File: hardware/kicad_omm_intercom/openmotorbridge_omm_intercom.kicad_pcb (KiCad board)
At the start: 2 copper layers, 60 x 30 mm, 19 parts, among them J1 TYPE-C-31-M-12_IP67, SW1 Power_MFB, SW2 Mesh_Group, SW3 Vol_Plus, SW4 Vol_Minus, U1 ESP32-C6-MINI-1U, U2 BQ24075RGTR, U3 XC6206P332MR, U4 ES8388, U5 ESP32-PICO-V3-02

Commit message: fix(hw): place J_HELMET on F.Cu top side facing right edge on PCBA 09 and 10
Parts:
- J_HELMET: moved to F.Cu
- turned J_HELMET to -90 degrees
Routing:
- net GND: track 53.5 -> 197.7 mm, vias 33 -> 26
- net BTN_VOL_DOWN: track 31.7 -> 51.5 mm, vias 4 -> 2
- net VCC_3V3: track 95.8 -> 77.2 mm, vias 12 -> 14
- net BTN_VOL_UP: track 25.1 -> 41.2 mm
- net WS2812_DATA: track 30.6 -> 45.7 mm
- net MIC_IN+: track 65.4 -> 57.7 mm, vias 3 -> 2
- net VBUS_5V: track 65.2 -> 58.0 mm, vias 4 -> 7
- net HP_OUT_R: track 51.4 -> 57.5 mm, vias 4 -> 6
- net USB_DN: track 18.4 -> 23.8 mm, vias 6 -> 4
- net CHG_STAT: track 27.5 -> 23.4 mm, vias 2 -> 4
- net HP_OUT_L: track 68.1 -> 71.3 mm, vias 4 -> 5
- net I2C_SDA: track 7.59 -> 9.79 mm
- net AGND_SPK: track 68.7 -> 66.7 mm, vias 2 -> 6
- net USB_DP: track 23.9 -> 25.8 mm, vias 6 -> 7
- net I2S_DOUT: track 12.7 -> 11.0 mm, vias 2 -> 0
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
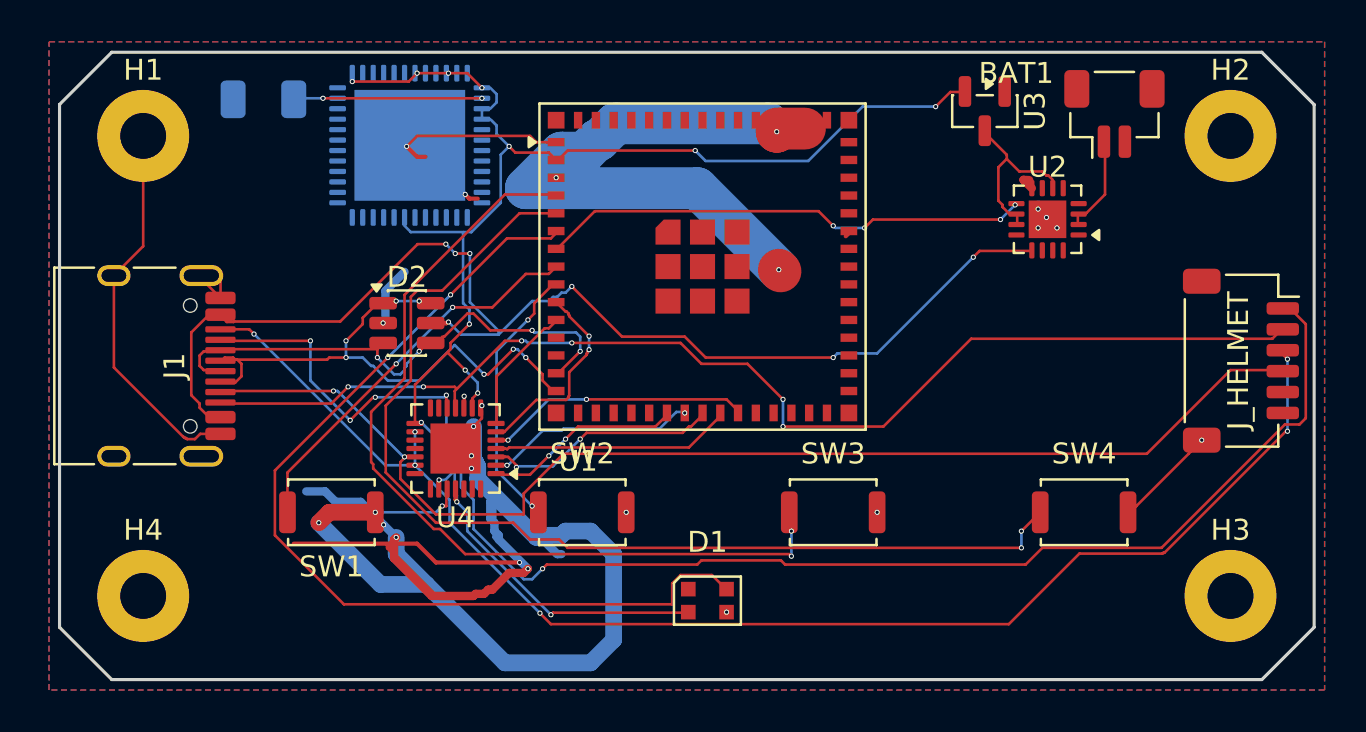
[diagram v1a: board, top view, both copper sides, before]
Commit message: fix(hardware): fleet-wide 7-PCBA remediation, schematic parity & doc alignment
- PCBA 01 (Central Box): Synchronized DTM-12 schematic and PCB routing, purged obsolete analog audio transformers/HD26 connector.
- PCBA 03 (Smart Cartridge): Verified Kelvin ground isolation on J_AUDIO_PWR, resolved U1.16 BAY_SELECT single net.
- PCBA 05 (Front Node): Mapped DW3110 UWB SPI/IRQ/RST to ESP32-S3 pads 30-35, connected MK1 I2S MEMS mic and Y_UWB crystal.
- PCBA 07 (Smart Keyfob): Connected 12 unrouted signals (SX1262 LoRa SPI, DRV2605L I2C, SWD, RTC crystal, buttons) to nRF52840 pads.
- PCBA 08 (Radar Sub-MCU): Synchronized J1.1 power rail to VCC_5V, connected Y1_UWB crystal to DW3110 pads 4 & 5.
- PCBA 09 & PCBA 10 (OMM 2.4 GHz & 446 MHz): Verified 4-layer stackup, BQ24075 ground ties, SA818 isolation, and vertical B.Cu J_HELMET orientation.
- Tools: Added verify_hardware_integrity.py with automated DRC/parity/single-net/floating-pad checks (all 7 PCBAs HEALTHY).
- Docs: Synchronized docs/de and docs/en hardware specifications, pinouts, and DTM-12 architecture.
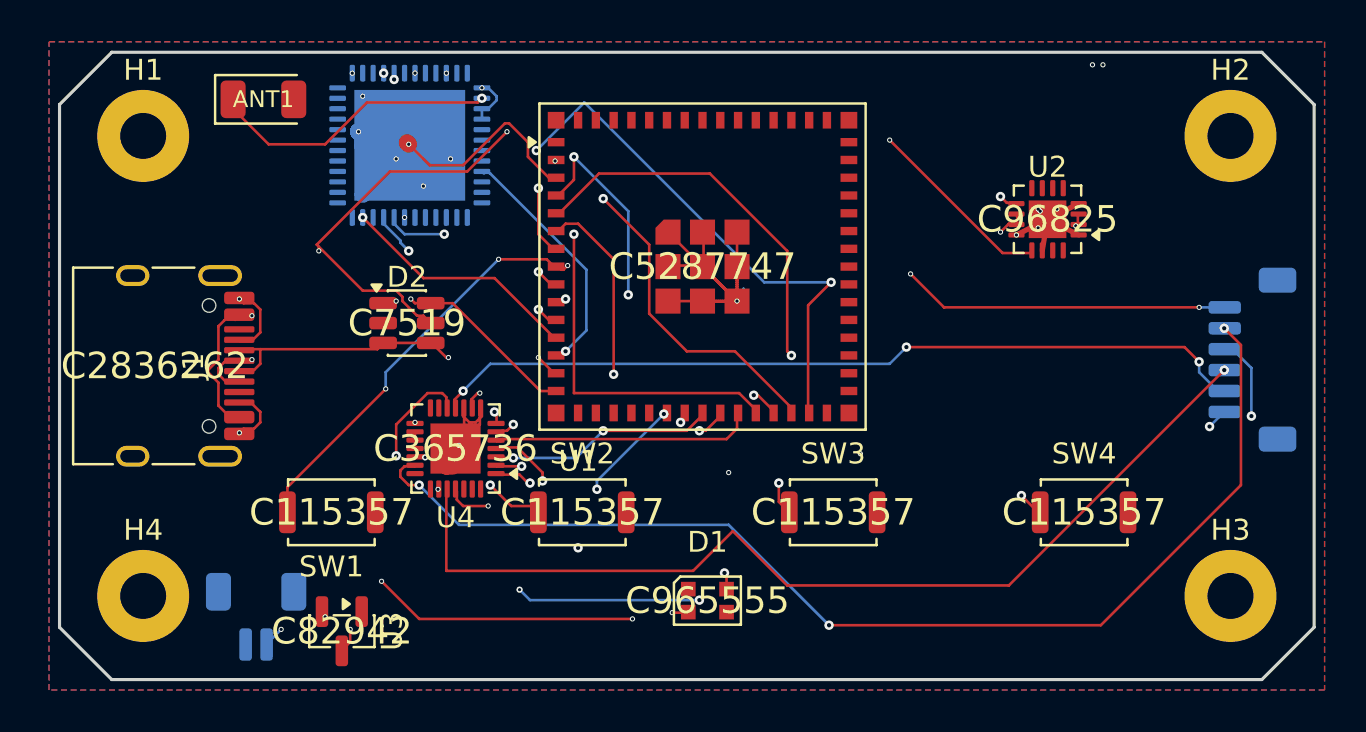
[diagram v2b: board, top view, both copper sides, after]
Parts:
- removed the J_HELMET at (126.5, 99.8)
- added J_HELMET: HELMET_AUDIO_6P, JST_SH_BM06B-SRSS-TB_1x06-1MP_P1.00mm_Vertical, B.Cu at (127.0, 99.7)
- ANT1: moved to F.Cu
- BAT1: moved to B.Cu
- SW1: value Power_MFB -> SW_1
- SW2: value Mesh_Group -> SW_2
- SW3: value Vol_Plus -> SW_3
- SW4: value Vol_Minus -> SW_4
- U3: value XC6206P332MR -> ME6211C33M5G
- moved BAT1 47.6 mm to (79.4, 112.0), turned to 180 degrees
- moved U3 39.6 mm to (83.5, 112.7)
- moved J1 0.90 mm to (74.5, 100.0)
- turned ANT1 to 180 degrees
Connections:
- net BTN_MESH renamed BTN_2
- net BTN_PWR renamed BTN_1
- net BTN_VOL_DOWN renamed BTN_4
- net BTN_VOL_UP renamed BTN_3
- D1 pad 1: (no net) -> GND
- J1 pad A5: HP_OUT_L -> GND
- J1 pad A8: MIC_IN+ -> (no net)
- J1 pad B5: HP_OUT_R -> GND
- J1 pad B8: AGND_SPK -> (no net)
- U1 pad 12: (no net) -> BT_BOOT
- U1 pad 13: (no net) -> BT_RESET
- U1 pad 26: (no net) -> BT_UART_CTS
- U1 pad 27: (no net) -> BT_UART_RTS
- U1 pad 28: (no net) -> BT_UART_TX
- U1 pad 29: (no net) -> BT_UART_RX
- U1 pad 54: (no net) -> GND
- U1 pad 55: (no net) -> GND
- U1 pad 56: (no net) -> GND
- U1 pad 57: (no net) -> GND
- U1 pad 58: (no net) -> GND
- U1 pad 59: (no net) -> GND
- U1 pad 60: (no net) -> GND
- U1 pad 61: (no net) -> GND
- U1 pad 62: (no net) -> GND
- U1 pad 63: (no net) -> GND
- U1 pad 64: (no net) -> GND
- U1 pad 65: (no net) -> GND
- U2 pad 1: NTC_TS -> GND
- U2 pad 12: ILIM -> GND
- U2 pad 16: ISET -> GND
- U2 pad 6: SYS_PWR -> GND
- U4 pad 11: HP_OUT_R -> AUDIO_OUT_R
- U4 pad 12: HP_OUT_L -> AUDIO_OUT_L
- U4 pad 16: AGND_SPK -> AGND
- U4 pad 17: VREF -> AGND
- U4 pad 18: MICBIAS -> AGND
- U4 pad 19: MIC_IN+ -> VOICE_IN
- U4 pad 20: AGND_SPK -> AGND_MIC
- U4 pad 24: GND -> AGND_SPK
- U5 pad : (no net) -> GND
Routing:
- net GND: track 197.7 -> 80.3 mm, vias 26 -> 17
- net HP_OUT_L: track 71.3 -> 0.00 mm, vias 5 -> 0
- net VCC_3V3: track 77.2 -> 19.1 mm, vias 14 -> 12
- net MIC_IN+: track 57.7 -> 0.00 mm, vias 2 -> 0
- net HP_OUT_R: track 57.5 -> 0.00 mm, vias 6 -> 0
- net AGND_MIC: track 0.00 -> 54.9 mm, vias 0 -> 3
- net AUDIO_OUT_L: track 0.00 -> 53.6 mm, vias 0 -> 3
- net VOICE_IN: track 0.00 -> 51.6 mm, vias 0 -> 4
- net VBAT: track 4.67 -> 49.6 mm, vias 0 -> 5
- net AUDIO_OUT_R: track 0.00 -> 39.5 mm, vias 0 -> 3
- net BT_UART_RX: track 0.00 -> 35.5 mm, vias 0 -> 3
- net SYS_PWR: track 7.94 -> 41.7 mm, vias 0 -> 3
- net BTN_1: track 18.9 -> 52.2 mm, vias 2 -> 5
- net BT_UART_TX: track 0.00 -> 28.0 mm, vias 0 -> 2
- net BT_UART_CTS: track 0.00 -> 25.9 mm, vias 0 -> 2
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- added copper zone on In1.Cu, net GND
- added copper zone on In2.Cu, net VCC_3V3
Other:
- copper layers 2 -> 4

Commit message: feat(hardware): achieve 100% 0-error DRC across all 7 official PCBAs and complete 4-layer Cartridge audio switching
- PCBA 01 (Central Box): Resolved keepout zone violation at U.FL ANT1, refilled zones (0 errors, 0 unconnected).
- PCBA 03 (Universal Smart Cartridge): Upgraded to 4 layers (JLC04161H), added SPDT analog/digital switch U4 (TS5A3159DBVR) on B.Cu and 10k pull-up R9 on F.Cu, routed symmetrical audio/OMM nets, schematic ERC 0 errors, DRC 0 errors, 0 unconnected.
- PCBA 05 (Front Node): 4-layer upgrade, solid GND plane, snapped OTTOCAST_FAULT_N (0 errors, 0 unconnected).
- PCBA 07 (Smart Keyfob): 4-layer upgrade, fixed Edge.Cuts arc alignment, routed U2 pad 23 (0 errors, 0 unconnected).
- PCBA 08 (Radar Sub-MCU), PCBA 09 (OMM 2.4 GHz), PCBA 10 (OMM 446 MHz): Verified 100% clean (0 errors, 0 unconnected).
- Added reproducibility tools: tools/sync_cartridge_sch.py and tools/remediate_pcba03.py.
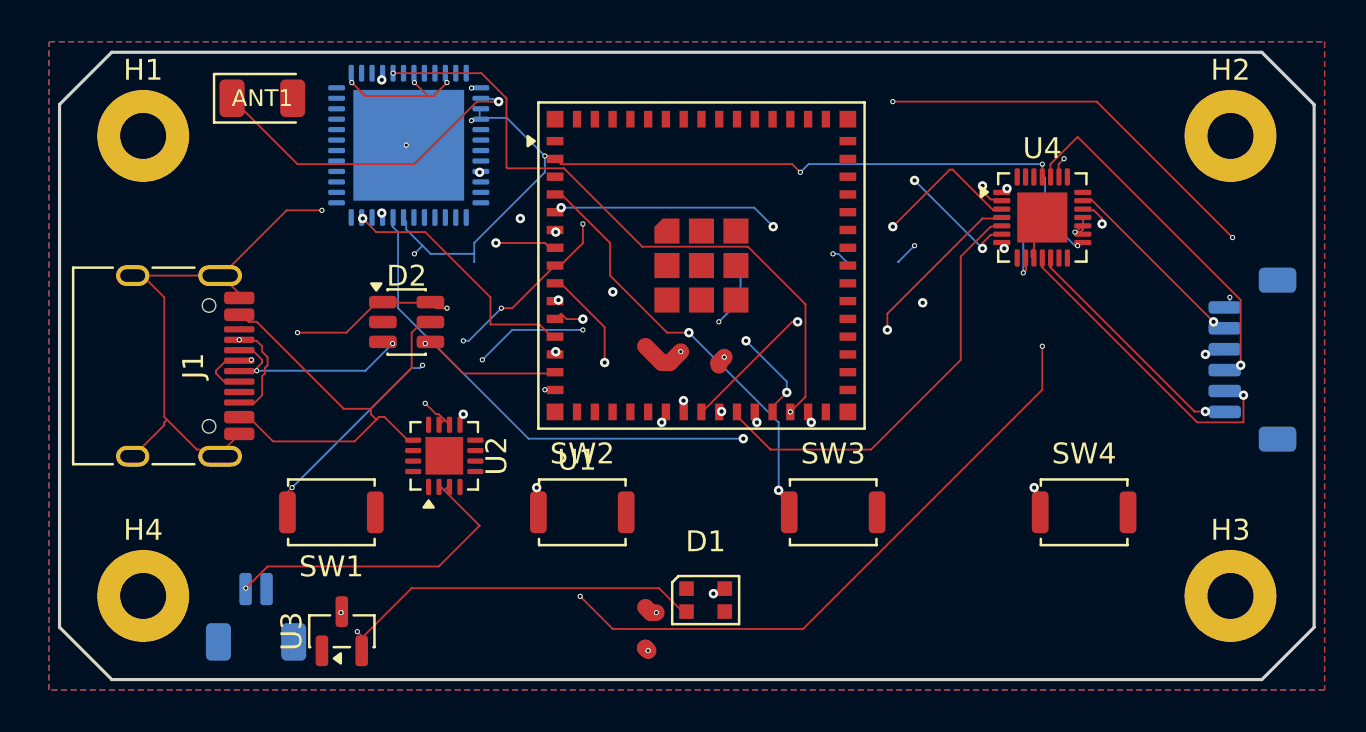
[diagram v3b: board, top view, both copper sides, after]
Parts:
- SW1: value SW_1 -> BTN_PTT
- SW2: value SW_2 -> BTN_MODE
- SW3: value SW_3 -> BTN_CH_UP
- SW4: value SW_4 -> BTN_CH_DOWN
- moved U2 31.0 mm to (88.4, 104.3), turned to 90 degrees
- moved U4 30.2 mm to (117.0, 92.9), turned to 0 degrees
- moved D1 0.09 mm to (100.9, 111.2)
- moved ANT1 0.07 mm to (79.7, 87.2)
- moved U1 0.07 mm to (100.7, 95.2)
- moved D2 0.05 mm to (86.6, 97.9)
- turned BAT1 to 0 degrees
- turned U3 to 90 degrees
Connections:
- J1 pad A1: GND -> PGND
- J1 pad A12: GND -> PGND
- J1 pad B1: GND -> PGND
- J1 pad B12: GND -> PGND
- J1 pad SH: GND -> PGND
- U1 pad 16: (no net) -> SA818_TXD
- U1 pad 17: (no net) -> SA818_RXD
- U1 pad 18: (no net) -> SA818_PTT
- U1 pad 19: (no net) -> SA818_SQL
- U1 pad 20: (no net) -> SA818_PWR_HL
- U4 pad 14: (no net) -> SA818_MIC_IN
- U4 pad 21: (no net) -> SA818_AF_OUT
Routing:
- net VCC_3V3: track 19.1 -> 100.3 mm, vias 12 -> 13
- net GND: track 80.3 -> 14.6 mm, vias 17 -> 6
- net PGND: track 0.00 -> 62.8 mm, vias 0 -> 2
- net AGND_MIC: track 54.9 -> 8.78 mm, vias 3 -> 1
- net AUDIO_OUT_L: track 53.6 -> 11.6 mm, vias 3 -> 1
- net VOICE_IN: track 51.6 -> 10.7 mm, vias 4 -> 2
- net AGND: track 0.95 -> 37.4 mm, vias 0 -> 3
- net VBAT: track 49.6 -> 15.5 mm, vias 5 -> 1
- net VBUS_5V: track 57.8 -> 23.9 mm, vias 4 -> 0
- net AGND_SPK: track 47.3 -> 17.6 mm
- net I2C_SCL: track 7.62 -> 35.5 mm
- net AUDIO_OUT_R: track 39.5 -> 15.5 mm, vias 3 -> 1
- net SYS_PWR: track 41.7 -> 22.7 mm, vias 3 -> 6
- net BT_UART_RX: track 35.5 -> 53.1 mm, vias 3 -> 2
- net I2C_SDA: track 8.61 -> 25.5 mm, vias 2 -> 3
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- added copper zone on In2.Cu, net SYS_PWR
- removed copper zone on In2.Cu, net VCC_3V3

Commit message: fix(omm-intercom): resolve net conflicts on PCBA 09 and pass prefab-gate check
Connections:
- J1 pad A1: PGND -> GND
- J1 pad A12: PGND -> GND
- J1 pad B1: PGND -> GND
- J1 pad B12: PGND -> GND
- J1 pad SH: PGND -> GND
- U1 pad 16: SA818_TXD -> (no net)
- U1 pad 17: SA818_RXD -> (no net)
- U1 pad 18: SA818_PTT -> (no net)
- U1 pad 19: SA818_SQL -> (no net)
- U1 pad 20: SA818_PWR_HL -> (no net)
- U4 pad 14: SA818_MIC_IN -> (no net)
- U4 pad 21: SA818_AF_OUT -> (no net)
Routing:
- net PGND: track 62.8 -> 0.00 mm, vias 2 -> 0
- net GND: track 14.6 -> 77.4 mm, vias 6 -> 8
